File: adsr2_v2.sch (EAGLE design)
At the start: 55 parts, among them IC1 LM324D, IC2 4052D, SW1_TIME TL2285 L, SW2_TRIG TL2285 L, T1 BC847, T2 BC857, T3 BC857, T4 BC847, T5 BC857

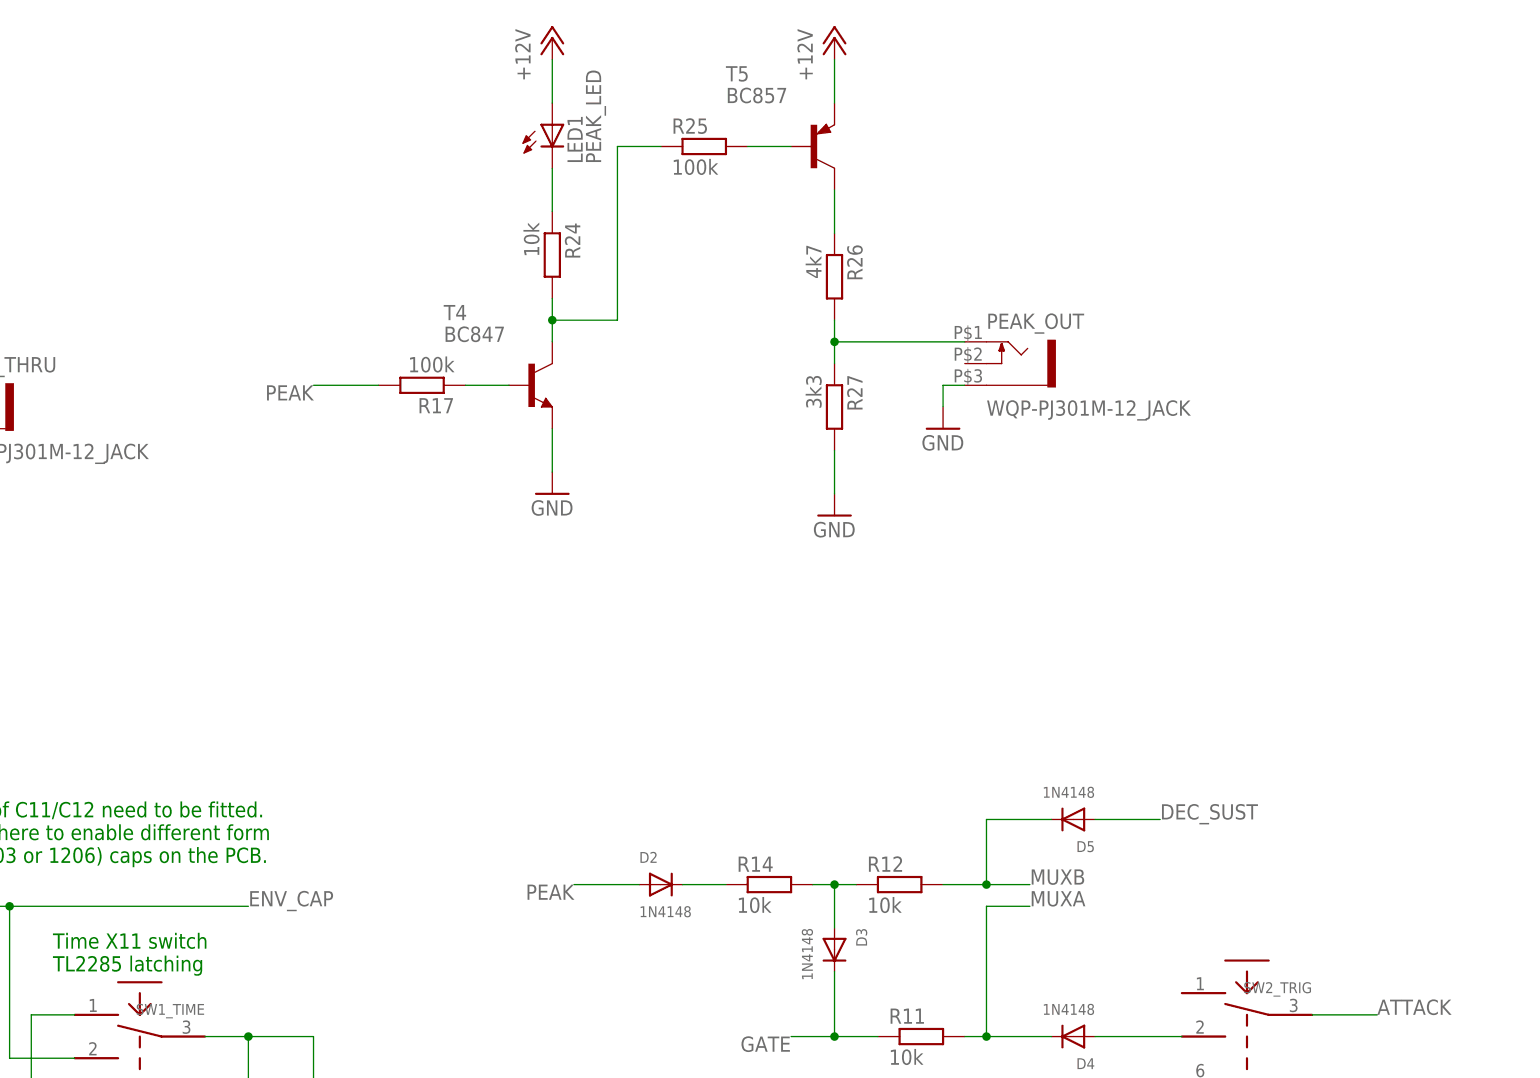
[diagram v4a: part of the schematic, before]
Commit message: Added circuit to make sure peak output pulse has at least a few ms duration. Changed peak output to behave like decay+sustain gate rather than just "attack done" trigger output.
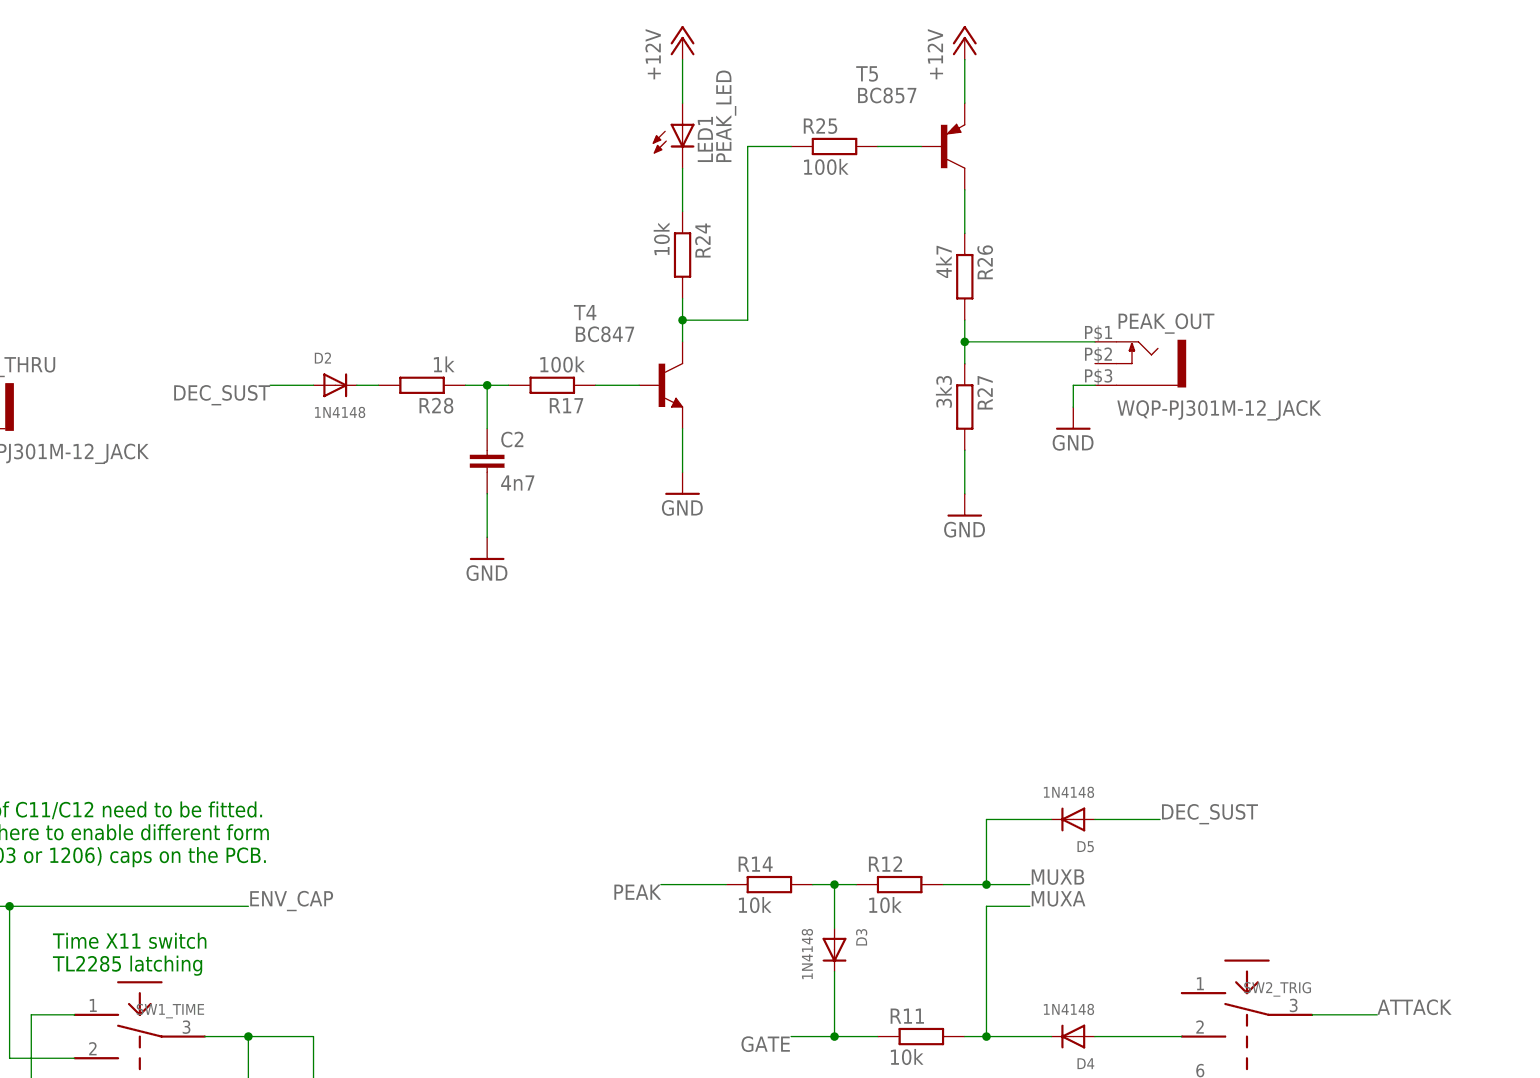
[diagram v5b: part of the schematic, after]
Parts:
- added C2: 4n7, rcl:C-EUC0603K
- added R28: 1k, rcl:R-EU_R0603
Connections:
- removed net N$29: D2.C, R14.1
- new net N$14: D2.C, R28.2
- new net N$20: C2.1, R17.2, R28.1
- net DEC_SUST: now also D2.A
- net GND: now also C2.2
- net PEAK: now also R14.1; no longer D2.A, R17.2
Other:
- moved on the sheet: D2, LED1, PEAK_OUT, R17, R24, R25, R26, R27, T4, T5

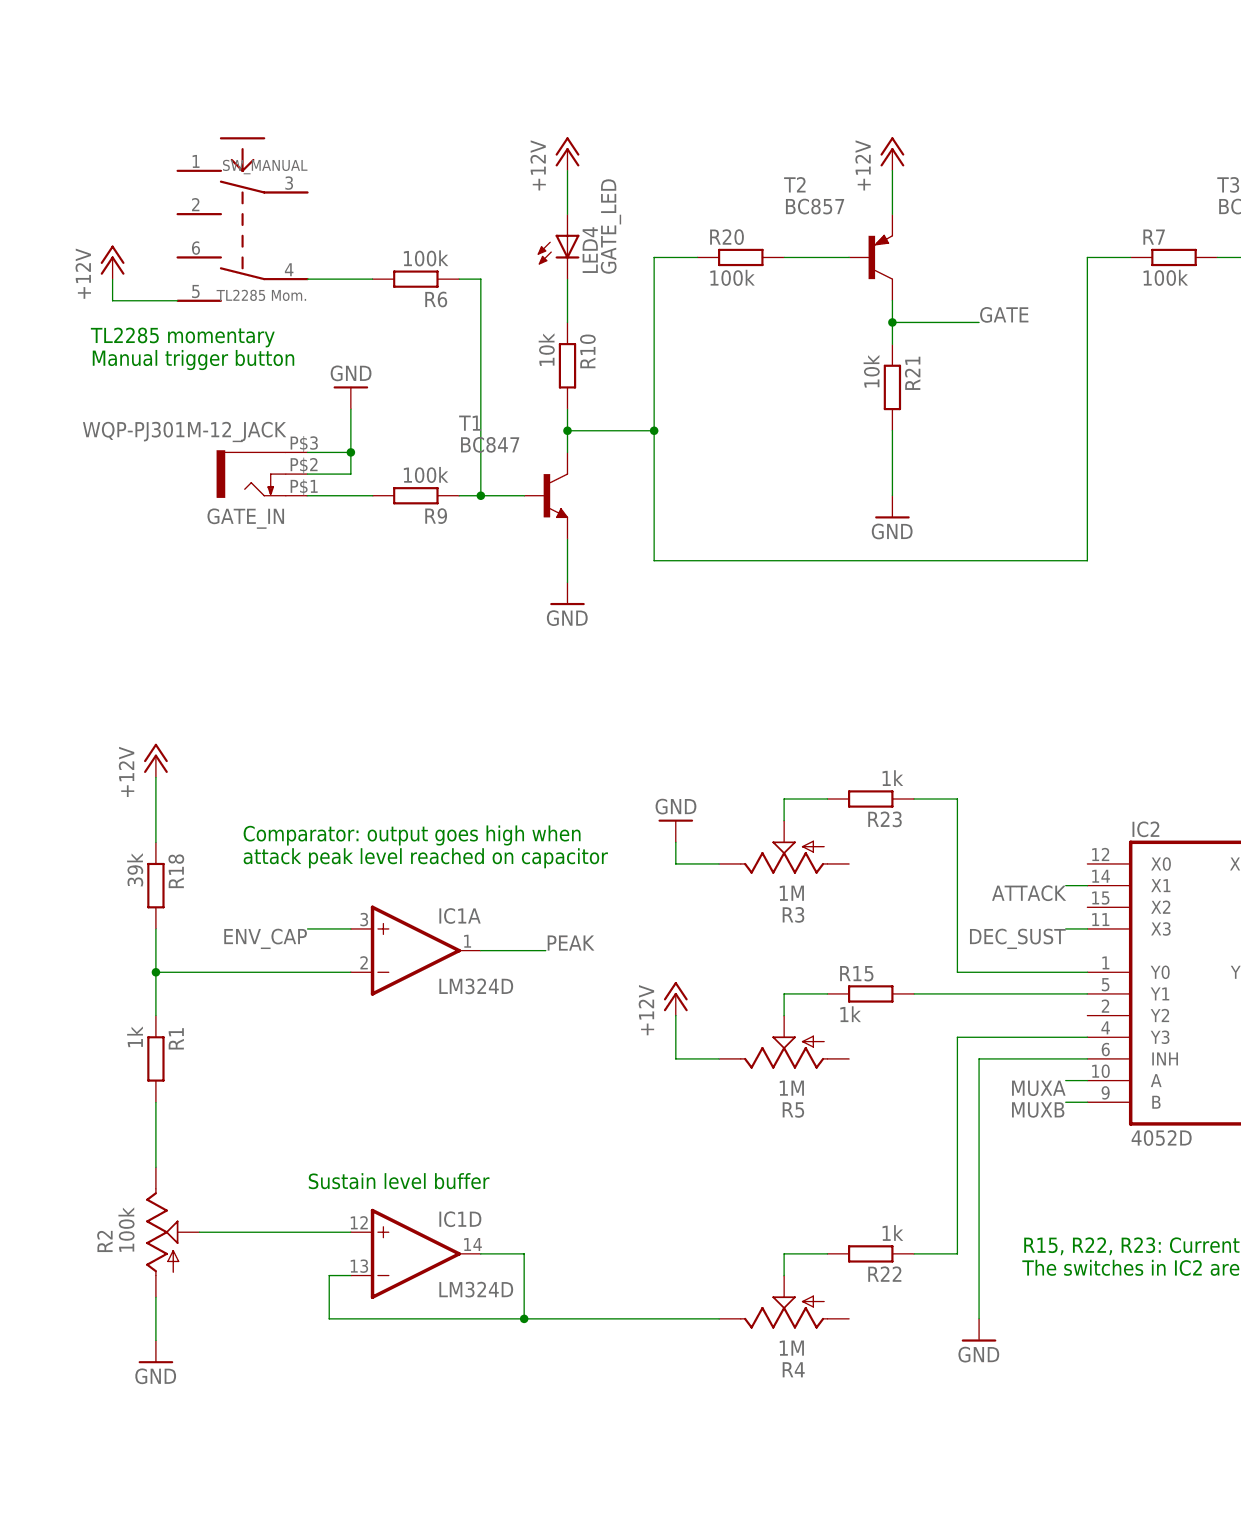
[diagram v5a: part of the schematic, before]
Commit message: Fixed direction of potentiometers. Added debouncing circuit for manual trig button. Updated date/version label.
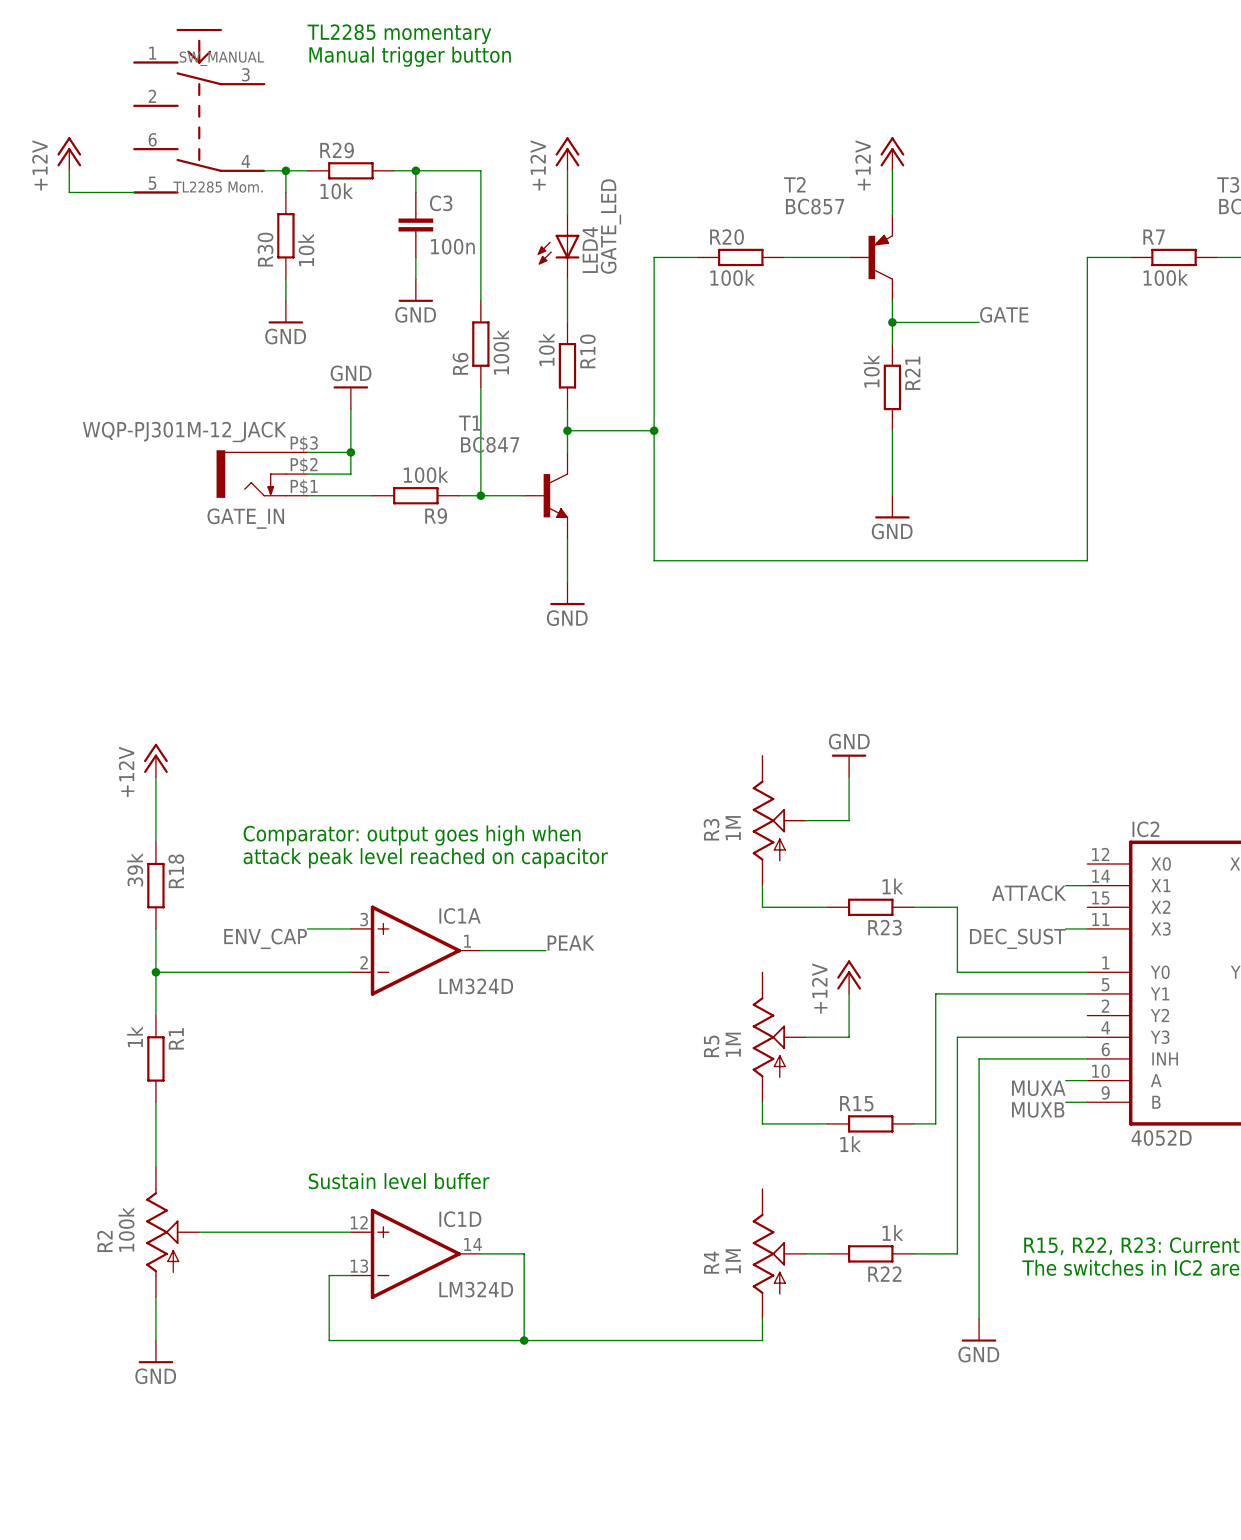
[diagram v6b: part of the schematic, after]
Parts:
- added C3: 100n, rcl:C-EUC0603K
- added R29, R30: 10k, rcl:R-EU_R0603
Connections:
- removed net N$28 (its old number): R15.1, R5.S
- new net N$15: C3.1, R29.2, R6.2
- new net N$25: R15.1, R5.A
- net +12V: now also R5.S; no longer R5.E
- net GND: now also C3.2, R3.S, R30.1; no longer R3.E
- net N$23: now also R3.A; no longer R3.S
- net N$4: now also R29.1, R30.2; no longer R6.2
- net N$7: now also R4.A; no longer R4.E
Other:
- moved on the sheet: R15, R23, R3, R4, R5, R6, SW_MANUAL
